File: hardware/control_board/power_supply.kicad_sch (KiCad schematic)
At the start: 29 parts, among them J5 5.5/2.5 mm, SW2 SW_SPST, U2 LMR38010SDDAR, U3 AMS1117-3.3

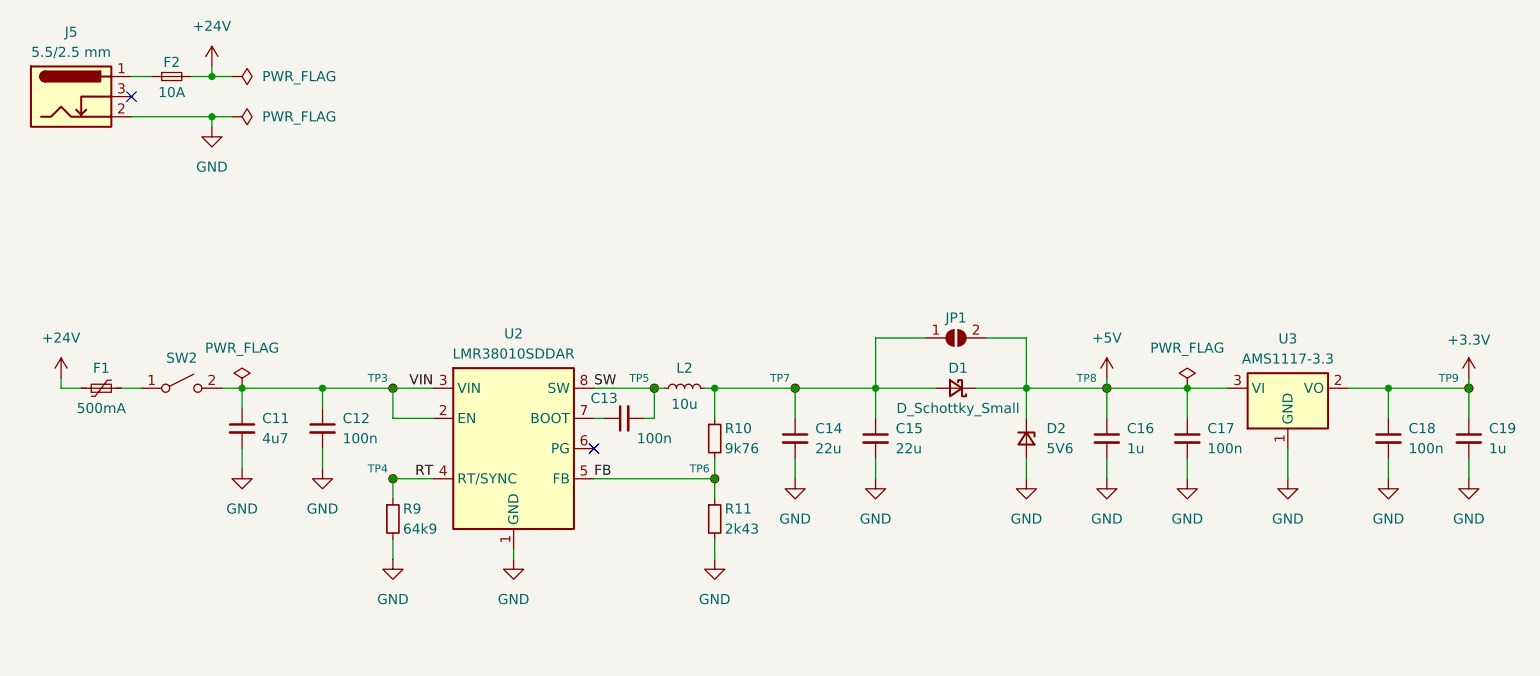
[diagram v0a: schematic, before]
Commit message: Adjust component values
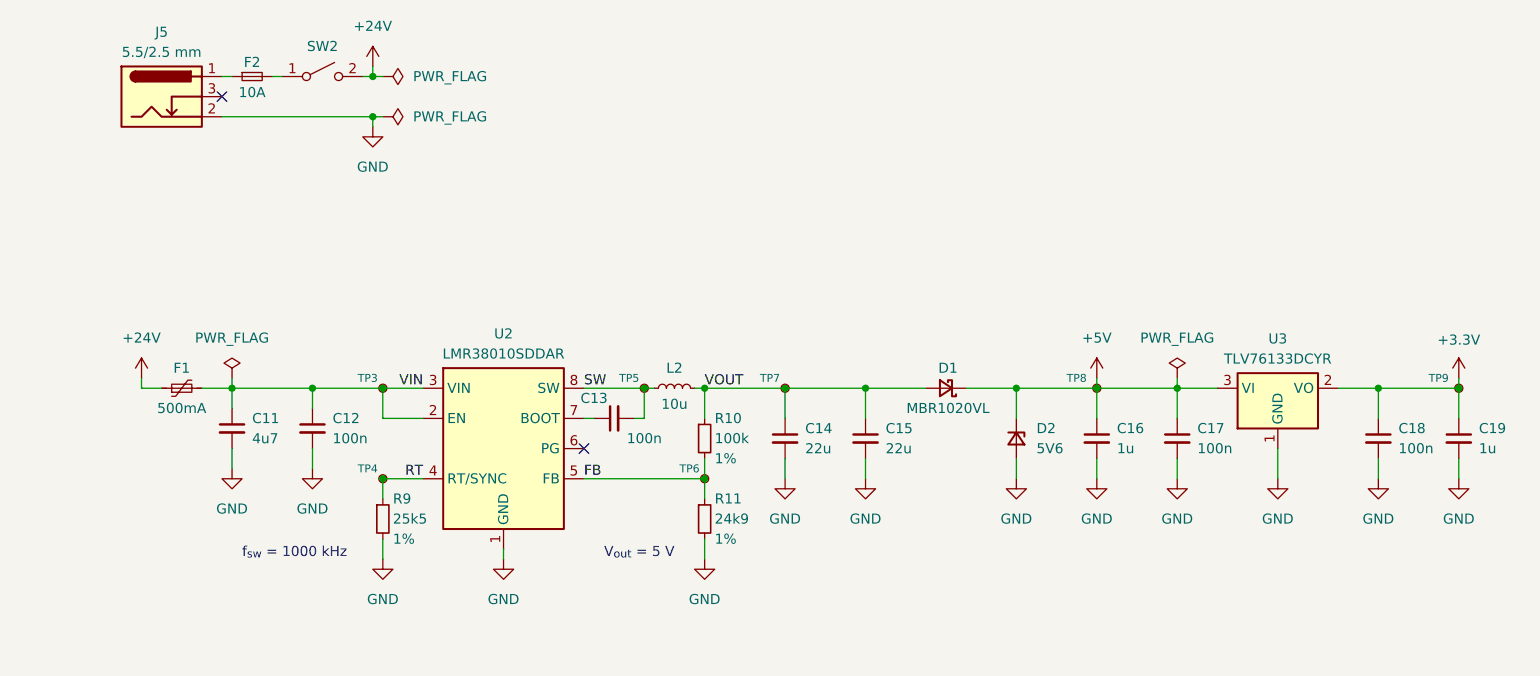
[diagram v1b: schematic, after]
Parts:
- removed JP1: SolderJumper_2_Open, symbol Jumper:SolderJumper_2_Open
- C11, C12, C13, C14, C15: footprint (none) -> Capacitor_SMD:C_0603_1608Metric
- D1: value D_Schottky_Small -> MBR1020VL; footprint (none) -> Diode_SMD:D_SOD-123F
- D2: footprint (none) -> Diode_SMD:D_0603_1608Metric
- R10: value 9k76 -> 100k; footprint (none) -> Resistor_SMD:R_0603_1608Metric; Tolerance (none) -> 1%
- R11: value 2k43 -> 24k9; footprint (none) -> Resistor_SMD:R_0603_1608Metric; Tolerance (none) -> 1%
- R9: value 64k9 -> 25k5; footprint (none) -> Resistor_SMD:R_0603_1608Metric; Tolerance (none) -> 1%
- U3: value AMS1117-3.3 -> TLV76133DCYR
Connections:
- net +24V: now also SW2.2 (B); no longer F2.2
- net VIN: now also F1.2; no longer SW2.2 (B)
- net at SW2.1 (A): now also F2.2; no longer F1.2
- net VOUT: now reaches C14.1, C15.1, D1.2 (A), L2.2, R10.1, TP7.1
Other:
- note added: "V_{out} = 5 V"
- note added: "f_{sw} = 1000 kHz"
- moved on the sheet: C11, C12, C13, C14, C15, C16, C17, C18, C19, D1, D2, F1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

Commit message: Assign footprints to components
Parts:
- removed J5: 5.5/2.5 mm, symbol Connector:Barrel_Jack_Switch
- added J5: 6.5/2mm, Connector_BarrelJack:BarrelJack_CUI_PJ-063AH_Horizontal, symbol Connector:Jack-DC
- D2: footprint Diode_SMD:D_0603_1608Metric -> Diode_SMD:D_SOD-123F; Component (none) -> BZT52H-C5V6,115
- F1: footprint Fuse:Fuse_0603_1608Metric -> Fuse:Fuse_1812_4532Metric; Component (none) -> 650-MINISMDC050F-2
- F2: footprint (none) -> Fuse:Fuseholder_Littelfuse_100_series_5x20mm
- L2: value 10u -> 15u; footprint (none) -> Inductor_SMD:L_Bourns-SRN6028; Component (none) -> SRN6028C-150M
- SW2: value SW_SPST -> Power; footprint (none) -> Connector_Wire:SolderWire-1sqmm_1x02_P5.4mm_D1.4mm_OD2.7mm; Component (none) -> 2M1-T2-1
- renumbered TP8 to TP10, TP9 to TP11, TP3 to TP5, TP4 to TP6, TP5 to TP7, TP6 to TP8, TP7 to TP9
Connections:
- net GND: now also J5.2
- net at F2.1: now also J5.1
- no-connect marks 2 -> 1
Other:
- moved on the sheet: C14, C15, C16, C17, C18, C19, D1, D2, L2, R10, R11, TP10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

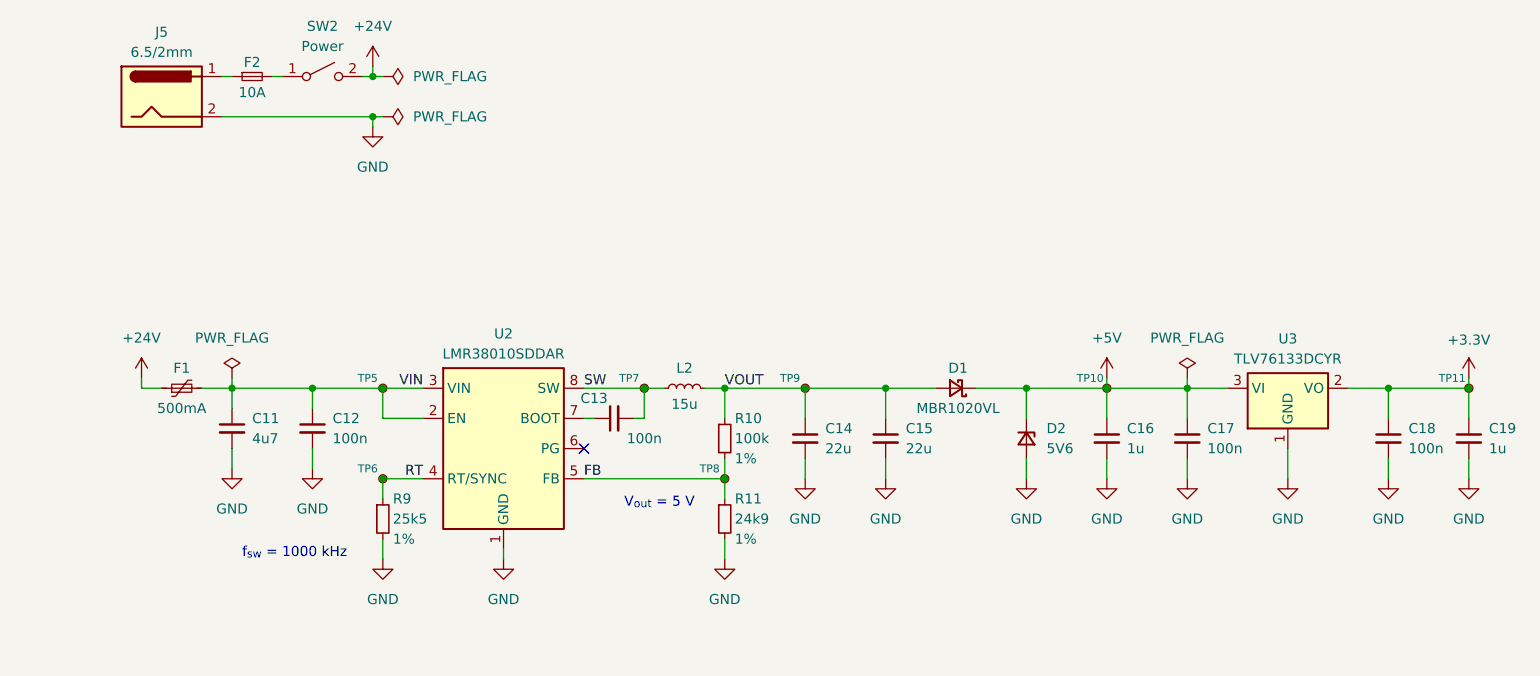
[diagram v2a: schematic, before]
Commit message: Place components on the control board PCB
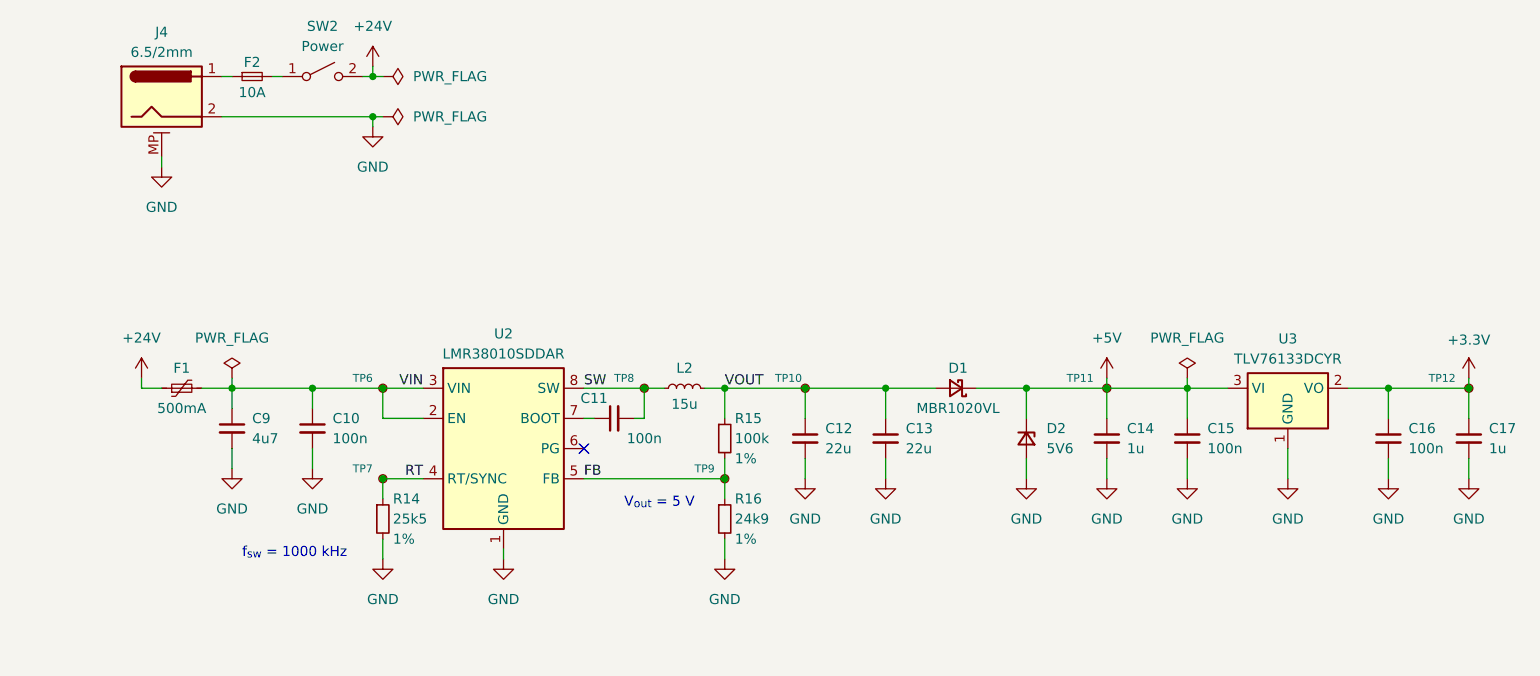
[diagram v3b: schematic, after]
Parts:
- F1: footprint Fuse:Fuse_1812_4532Metric -> Local_Library:MINISMDCx
- F2: footprint Fuse:Fuseholder_Littelfuse_100_series_5x20mm -> Fuse:Fuseholder_Cylinder-5x20mm_Schurter_0031_8201_Horizontal_Open
- J4: renamed from J5; symbol Connector:Jack-DC -> PJ-063AH:PJ-063AH
- L2: footprint Inductor_SMD:L_Bourns-SRN6028 -> Local_Library:SRN6028Cx
- renumbered C12 to C10, C13 to C11, C14 to C12, C15 to C13, C16 to C14, C17 to C15, C18 to C16, C19 to C17, C11 to C9, R9 to R14, R10 to R15, R11 to R16, TP9 to TP10, TP10 to TP11, TP11 to TP12, TP5 to TP6, TP6 to TP7, TP7 to TP8, TP8 to TP9
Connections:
- net GND: now also J4.MP (MountPin)

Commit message: Route front panel PCB tracks
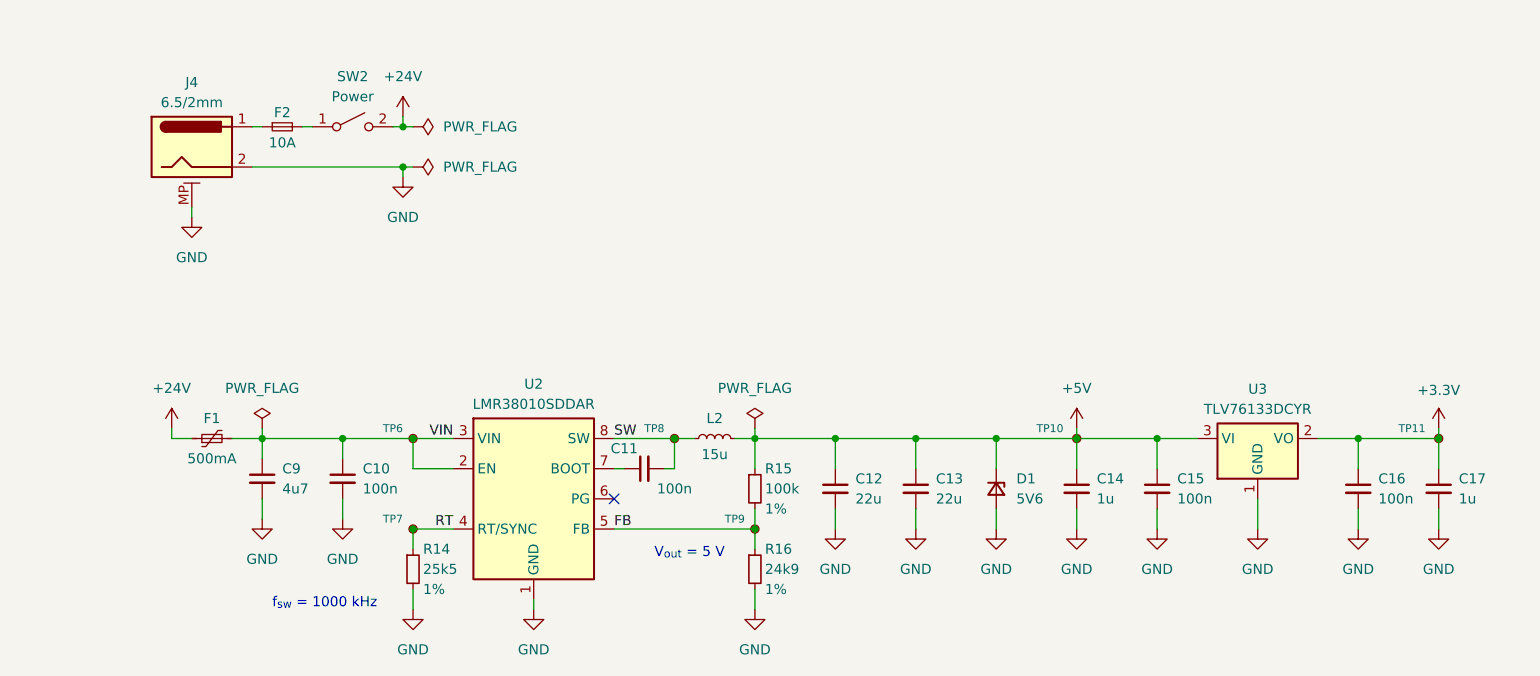
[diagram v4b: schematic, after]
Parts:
- removed D1: MBR1020VL, Diode_SMD:D_SOD-123F, symbol Device:D_Schottky_Small
- removed TP10: TestPoint_Small, TestPoint:TestPoint_Pad_D1.0mm, symbol Connector:TestPoint_Small
- TP10: renamed from TP11; now left out of the parts list
- TP11: renamed from TP12; now left out of the parts list
- TP6, TP7, TP8, TP9: now left out of the parts list
- renumbered D2 to D1
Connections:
- net VOUT is gone; now on net +5V: C12.1, C13.1, L2.2, R15.1
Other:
- moved on the sheet: C10, C11, C12, C13, C14, C15, C16, C17, C9, D1, F1, F2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

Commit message: Route control board PCB tracks
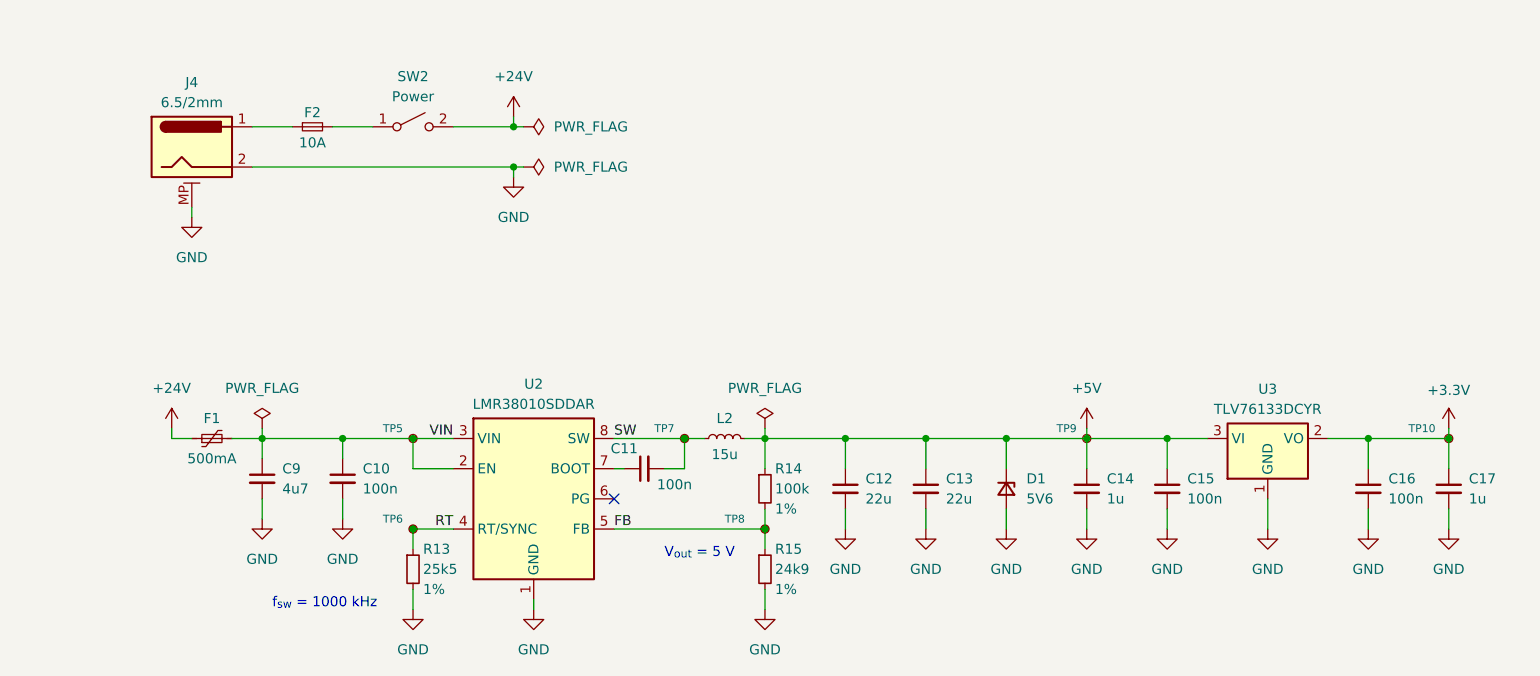
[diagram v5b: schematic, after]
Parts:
- renumbered R14 to R13, R15 to R14, R16 to R15, TP11 to TP10, TP6 to TP5, TP7 to TP6, TP8 to TP7, TP9 to TP8, TP10 to TP9
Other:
- moved on the sheet: C12, C13, C14, C15, C16, C17, D1, F2, L2, R14, R15, SW2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

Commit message: Fix DRC errors
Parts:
- SW2: footprint Connector_Wire:SolderWire-1sqmm_1x02_P5.4mm_D1.4mm_OD2.7mm -> Local_Library:SwitchWireRelief
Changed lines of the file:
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@@
       (effects (font (size 1.27 1.27)))
     )
-    (property "Footprint" "Connector_Wire:SolderWire-1sqmm_1x02_P5.4mm_D1.4mm_OD2.7mm" (at 100.33 59.69 0)
+    (property "Footprint" "Local_Library:SwitchWireRelief" (at 100.33 59.69 0)
       (effects (font (size 1.27 1.27)) hide)
     )

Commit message: Minor layout adjustments
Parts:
- C10: value 100n -> 100n/35V
- C9: value 4u7 -> 4u7/35V
- J4: footprint Connector_BarrelJack:BarrelJack_CUI_PJ-063AH_Horizontal -> Local_Library:BarrelJack_CUI_PJ-063AH_Horizontal
- L2: symbol Device:L_Small -> Device:L
- SW2: Component 2M1-T2-1 -> MTS-1
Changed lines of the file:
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@@
+    (stroke (width 0) (type default))
+  )
+  (wire (pts (xy 143.51 99.06) (xy 144.78 99.06))
     (stroke (width 0) (type default))
   )
@@
     (stroke (width 0) (type default))
   )
-  (wire (pts (xy 142.24 99.06) (xy 144.78 99.06))
-    (stroke (width 0) (type default))
-  )
   (wire (pts (xy 100.33 102.87) (xy 100.33 99.06))
     (stroke (width 0) (type default))
@@
     (stroke (width 0) (type default))
   )
-  (wire (pts (xy 134.62 99.06) (xy 137.16 99.06))
-    (stroke (width 0) (type default))
-  )
   (wire (pts (xy 185.42 102.87) (xy 185.42 99.06))
     (stroke (width 0) (type default))
@@
   )
   (wire (pts (xy 81.28 106.68) (xy 81.28 109.22))
+    (stroke (width 0) (type default))
+  )
+  (wire (pts (xy 134.62 99.06) (xy 135.89 99.06))
     (stroke (width 0) (type default))
   )
@@
       (effects (font (size 1.27 1.27)) hide)
     )
-    (property "Component" "2M1-T2-1" (at 100.33 59.69 0)
+    (property "Component" "MTS-1" (at 100.33 59.69 0)
       (effects (font (size 1.27 1.27)) hide)
     )
@@
   )
   (symbol (lib_id "Device:C_Small") (at 91.44 104.14 0) (unit 1)
-    (in_bom yes) (on_board yes) (dnp no) (fields_autoplaced)
+    (in_bom yes) (on_board yes) (dnp no)
     (property "Reference" "C10" (at 93.98 102.8763 0)
       (effects (font (size 1.27 1.27)) (justify left))
     )
-    (property "Value" "100n" (at 93.98 105.4163 0)
+    (property "Value" "100n/35V" (at 92.71 106.6863 0)
       (effects (font (size 1.27 1.27)) (justify left))
     )
@@
       (effects (font (size 1.27 1.27)) (justify top))
     )
-    (property "Footprint" "Connector_BarrelJack:BarrelJack_CUI_PJ-063AH_Horizontal" (at 72.39 79.756 0)
+    (property "Footprint" "Local_Library:BarrelJack_CUI_PJ-063AH_Horizontal" (at 72.39 79.756 0)
       (effects (font (size 1.27 1.27)) hide)
     )
@@
     )
   )
-  (symbol (lib_id "Device:L_Small") (at 139.7 99.06 90) (unit 1)
+  (symbol (lib_id "Device:L") (at 139.7 99.06 90) (unit 1)
     (in_bom yes) (on_board yes) (dnp no)
     (property "Reference" "L2" (at 139.7 96.52 90)
@@
   )
   (symbol (lib_id "Device:C_Small") (at 81.28 104.14 0) (unit 1)
-    (in_bom yes) (on_board yes) (dnp no) (fields_autoplaced)
+    (in_bom yes) (on_board yes) (dnp no)
     (property "Reference" "C9" (at 83.82 102.8763 0)
       (effects (font (size 1.27 1.27)) (justify left))
     )
-    (property "Value" "4u7" (at 83.82 105.4163 0)
-      (effects (font (size 1.27 1.27)) (justify left))
-    )
+    (property "Value" "4u7/35V" (at 82.55 106.6863 0)
+      (effects (font (size 1.27 1.27)) (justify left))
+    )

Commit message: Cleanup the project
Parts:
- C10: value 100n/35V -> 100n; Rated Voltage (none) -> 35V
- C9: value 4u7/35V -> 4u7; Rated Voltage (none) -> 35V
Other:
- moved on the sheet: C10, C11, C9, F1, F2, J4, L2, R13, R14, R15, SW2, TP5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
